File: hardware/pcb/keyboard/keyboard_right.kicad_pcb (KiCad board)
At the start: 2 copper layers, 133.8 x 110.4 mm, 118 parts, among them J1 SM04B-SRSS-TB, J2 PJ320D, J3 HRO_TYPE-C-31-M-12, J4 HRS_FH34SRJ-06S-0.5SH(50), SW29 PTS845, U1 74HC4051, U2 OPA350UA, U3 PRTR5V0U2X, U4 XC6220B331MR-G, U5 STM32G431KBTx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

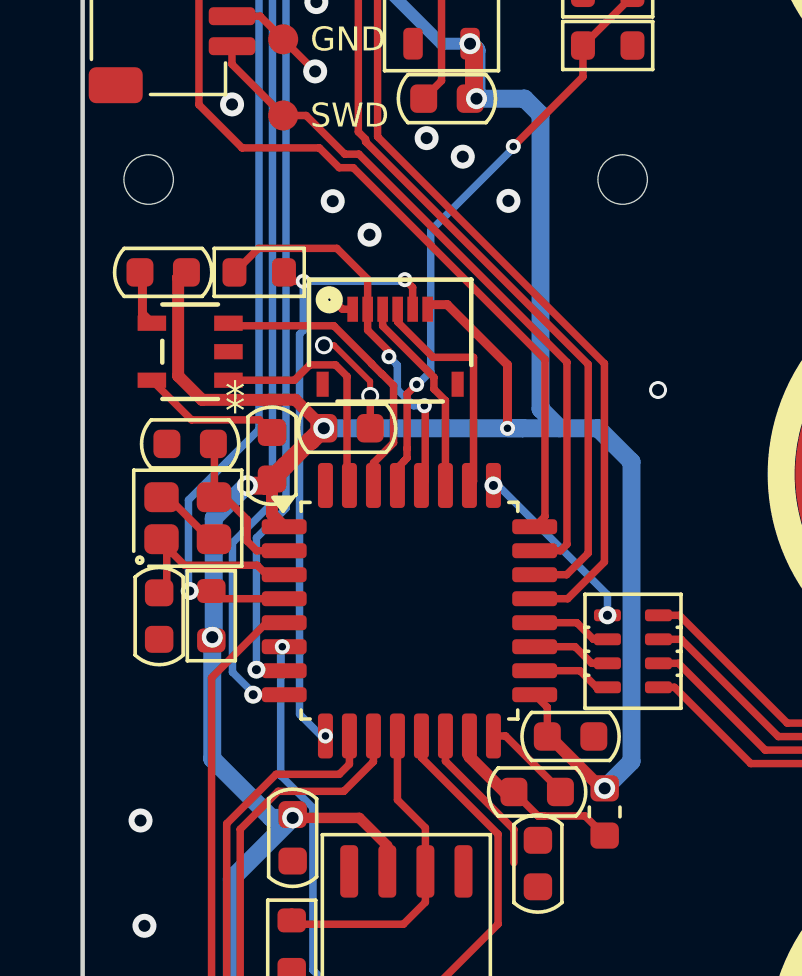
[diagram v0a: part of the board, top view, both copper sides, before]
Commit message: add pull up register for I2C.
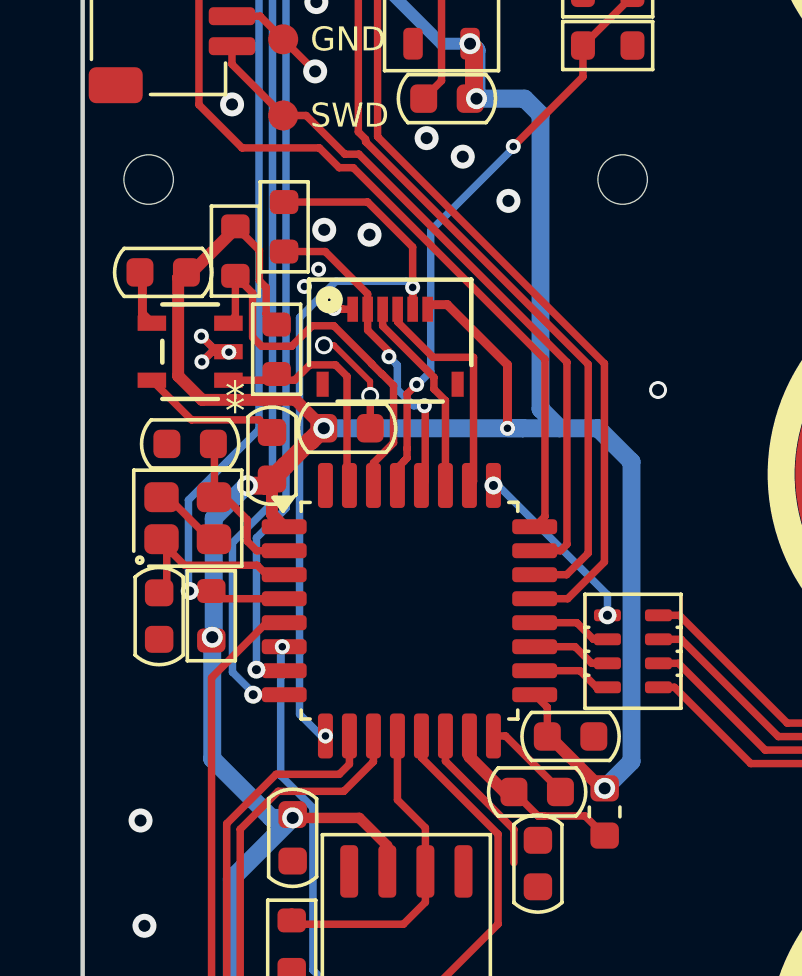
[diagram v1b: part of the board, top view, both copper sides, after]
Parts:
- added R10: 10k, PCM_Resistor_SMD_AKL:R_0603_1608Metric, F.Cu at (76.7, 76.8)
- added R9: 10k, PCM_Resistor_SMD_AKL:R_0603_1608Metric, F.Cu at (75.3, 73.6)
- moved R8 1.73 mm to (77.0, 72.8), turned to 90 degrees
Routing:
- net +3V3: track 110.8 -> 116.9 mm
- net ACCS_1: track 20.9 -> 26.4 mm, vias 3 -> 2
- net GND: track 42.7 -> 46.4 mm, vias 30 -> 35
- net I2C1_SDA: track 9.78 -> 13.5 mm
- net ACCS_4: track 13.0 -> 10.6 mm

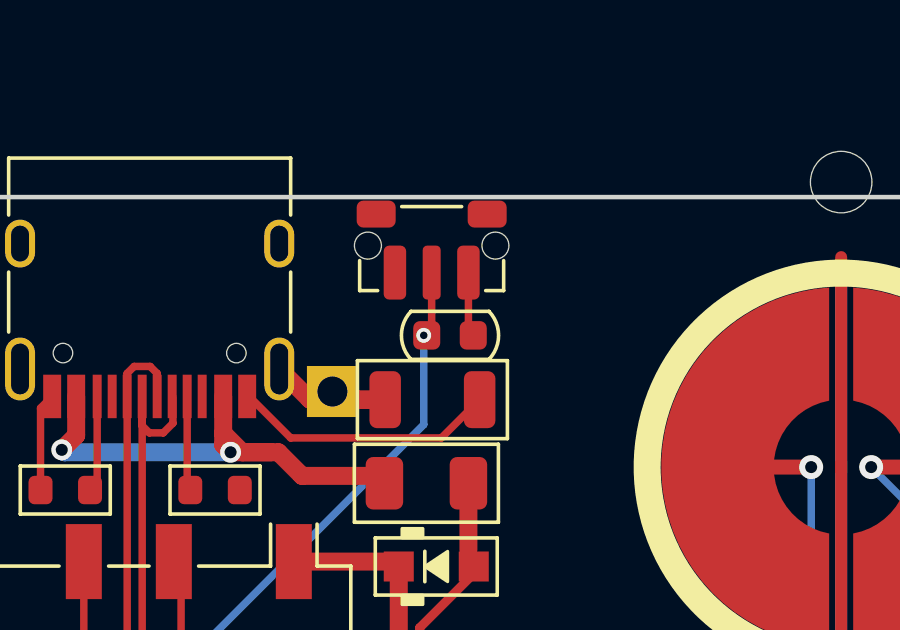
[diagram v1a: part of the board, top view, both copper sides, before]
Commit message: fix acc connection.
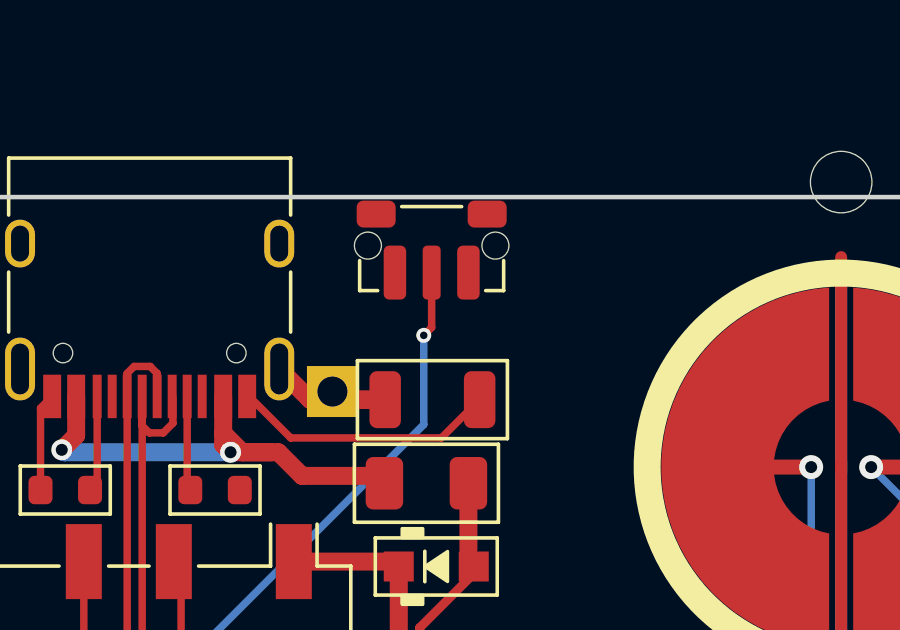
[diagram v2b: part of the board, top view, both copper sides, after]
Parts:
- removed C1: 0.1uF, PCM_Capacitor_SMD_AKL:C_0603_1608Metric
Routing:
- net GND: track 46.4 -> 44.6 mm
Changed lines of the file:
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@@
 		)
 	)
-	(footprint "PCM_Capacitor_SMD_AKL:C_0603_1608Metric"
-		(layer "F.Cu")
-		(at 86.961 38.609 180)
-		(descr "Capacitor SMD 0603 (1608 Metric), square (rectangular) end terminal, IPC_7351 nominal, (Body size source: IPC-SM-782 page 76, https://www.pcb-3d.com/wordpress/wp-content/uploads/ipc-sm-782a_amendment_1_and_2.pdf), Alternate KiCad Library")
-		(tags "capacitor")
-		(property "Reference" "C1"
-			(at 0 -1.43 180)
-			(layer "F.SilkS")
-			(hide yes)
-			(effects
-				(font
-					(size 1 1)
-					(thickness 0.15)
-				)
-			)
-		)
-		(property "Value" "0.1uF"
-			(at 0 1.43 180)
-			(layer "F.Fab")
-			(hide yes)
-			(effects
-				(font
-					(size 1 1)
-					(thickness 0.15)
-				)
-			)
-		)
-		(property "Datasheet" "~"
-			(at 0 0 180)
-			(unlocked yes)
-			(layer "F.Fab")
-			(hide yes)
-			(effects
-				(font
-					(size 1.27 1.27)
-					(thickness 0.15)
-				)
-			)
-		)
-		(property "Description" ""
-			(at 0 0 180)
-			(unlocked yes)
-			(layer "F.Fab")
-			(hide yes)
-			(effects
-				(font
-					(size 1.27 1.27)
-					(thickness 0.15)
-				)
-			)
-		)
-		(property "LCSC" "C307331"
-			(at 0 0 0)
-			(layer "F.Fab")
-			(hide yes)
-			(effects
-				(font
-					(size 1 1)
-					(thickness 0.15)
-				)
-			)
-		)
-		(property ki_fp_filters "C_*")
-		(sheetname "/")
-		(sheetfile "keyboard_right.kicad_sch")
-		(attr smd)
-		(fp_line
-			(start 1.3 -0.800002)
-			(end -1.3 -0.8)
-			(stroke
-				(width 0.12)
-				(type solid)
-			)
-			(layer "F.SilkS")
-		)
-		(fp_line
-			(start -1.3 0.800002)
-			(end 1.3 0.8)
-			(stroke
-				(width 0.12)
-				(type solid)
-			)
-			(layer "F.SilkS")
-		)
-		(fp_arc
-			(start 1.3 -0.800002)
-			(mid 1.619939 -0.000001)
-			(end 1.3 0.8)
-			(stroke
-				(width 0.12)
-				(type solid)
-			)
-			(layer "F.SilkS")
-		)
-		(fp_arc
-			(start -1.3 0.800002)
-			(mid -1.619939 0.000001)
-			(end -1.3 -0.8)
-			(stroke
-				(width 0.12)
-				(type solid)
-			)
-			(layer "F.SilkS")
-		)
-		(fp_line
-			(start 1.48 0.73)
-			(end -1.48 0.73)
-			(stroke
-				(width 0.05)
-				(type solid)
-			)
-			(layer "F.CrtYd")
-		)
-		(fp_line
-			(start 1.48 -0.73)
-			(end 1.48 0.73)
-			(stroke
-				(width 0.05)
-				(type solid)
-			)
-			(layer "F.CrtYd")
-		)
-		(fp_line
-			(start -1.48 0.73)
-			(end -1.48 -0.73)
-			(stroke
-				(width 0.05)
-				(type solid)
-			)
-			(layer "F.CrtYd")
-		)
-		(fp_line
-			(start -1.48 -0.73)
-			(end 1.48 -0.73)
-			(stroke
-				(width 0.05)
-				(type solid)
-			)
-			(layer "F.CrtYd")
-		)
-		(fp_line
-			(start 0.8 0.4)
-			(end -0.8 0.4)
-			(stroke
-				(width 0.1)
-				(type solid)
-			)
-			(layer "F.Fab")
-		)
-		(fp_line
-			(start 0.8 -0.4)
-			(end 0.8 0.4)
-			(stroke
-				(width 0.1)
-				(type solid)
-			)
-			(layer "F.Fab")
-		)
-		(fp_line
-			(start -0.8 0.4)
-			(end -0.8 -0.4)
-			(stroke
-				(width 0.1)
-				(type solid)
-			)
-			(layer "F.Fab")
-		)
-		(fp_line
-			(start -0.8 -0.4)
-			(end 0.8 -0.4)
-			(stroke
-				(width 0.1)
-				(type solid)
-			)
-			(layer "F.Fab")
-		)
-		(fp_text user "${REFERENCE}"
-			(at 0 0 180)
-			(layer "F.Fab")
-			(effects
-				(font
-					(size 0.4 0.4)
-					(thickness 0.06)
-				)
-			)
-		)
-		(pad "1" smd roundrect
-			(at -0.775 0 180)
-			(size 0.9 0.95)
-			(layers "F.Cu" "F.Mask" "F.Paste")
-			(roundrect_rratio 0.25)
-			(net 19 "GND")
-			(pintype "passive")
-		)
-		(pad "2" smd roundrect
-			(at 0.775 0 180)
-			(size 0.9 0.95)
-			(layers "F.Cu" "F.Mask" "F.Paste")
-			(roundrect_rratio 0.25)
-			(net 43 "/NRST")
-			(pintype "passive")
-		)
-		(embedded_fonts no)
-		(model "${KICAD6_3DMODEL_DIR}/Capacitor_SMD.3dshapes/C_0603_1608Metric.wrl"
-			(offset
-				(xyz 0 0 0)
-			)
-			(scale
-				(xyz 1 1 1)
-			)
-			(rotate
-				(xyz 0 0 0)
-			)
-		)
-	)
 	(footprint "ec_parts:ecs_pad_no_ring"
 		(layer "F.Cu")
@@
 	)
 	(segment
-		(start 87.575 36.517)
-		(end 87.575 38.348)
-		(width 0.25)
-		(layer "F.Cu")
-		(net 19)
-	)
-	(segment
 		(start 76.561 79.606)
 		(end 76.141 79.186)
@@
 		(width 0.25)
 		(layer "F.Cu")
+		(net 43)
+	)
+	(segment
+		(start 86.35 38.345)
+		(end 86.086 38.609)
+		(width 0.25)
+		(layer "F.Cu")

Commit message: update schema.
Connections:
- net ACCS_1 renamed PA4
- net ACCS_2 renamed PB3
- net ACCS_3 renamed PB4
- net ACCS_4 renamed PB5

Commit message: Generate production files.
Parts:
- D1: value 1N5819 -> BAT60B
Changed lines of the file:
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@@
 	(paper "A4")
 	(title_block
-		(title "Corne EEC")
-		(date "2023-07-18")
-		(rev "1.0")
-		(comment 1 "Copyright © 2023")
+		(title "Corne EEC - Keyboard Right")
+		(date "2025-09-18")
+		(rev "2.0")
 		(comment 2 "MIT License")
 	)
@@
 			)
 		)
-		(property "Value" "1N5819"
+		(property "Value" "BAT60B"
 			(at 0.1 1.9 0)
 			(layer "F.Fab")
@@
 			)
 		)
-		(property "Comment" ""
+		(property "Comment" "Alternative: 1N5819"
 			(at 0 0 0)
 			(layer "F.Fab")
@@
 			(unlocked yes)
 			(layer "F.SilkS")
+			(hide yes)
 			(effects
 				(font
@@
 			(unlocked yes)
 			(layer "F.Fab")
+			(hide yes)
 			(effects
 				(font
@@
 		(fp_text user "*"
 			(at -1.5 -1.5 180)
-			(unlocked yes)
 			(layer "F.SilkS")
 			(effects
@@
 		(fp_text user "*"
 			(at -1.5 -1.5 180)
+			(unlocked yes)
 			(layer "F.SilkS")
 			(effects
@@
 			)
 		)
-		(property "Comment" ""
+		(property "Comment" "Alternative: AP2112K"
 			(at 0 0 0)
 			(layer "F.Fab")

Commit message: Rev 2.1
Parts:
- removed H18, H19: ~, ec_parts:SMT-SO-M1.6-screwhole_only
- J4: footprint ec_parts:CONN6x1_FH34SRJ-6S-0.5SH50_HIR -> ec_parts:CONN6x1_FH12S-6S-1SH55
- moved R5 15.4 mm to (87.7, 51.3), turned to 0 degrees
- moved R4 15.4 mm to (87.7, 49.5)
- moved J4 11.1 mm to (86.5, 67.1), turned to 90 degrees
- moved C9 9.98 mm to (85.7, 59.1), turned to 90 degrees
- moved C8 6.74 mm to (83.0, 55.8)
- moved U4 6.74 mm to (82.8, 58.8)
- moved TP1 5.21 mm to (73.2, 65.1)
- moved J1 5.00 mm to (73.2, 60.7)
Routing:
- net PB6: track 19.0 -> 36.7 mm
- net VBUS: track 21.8 -> 5.80 mm
- net PB5: track 10.6 -> 26.6 mm
- net PB4: track 6.74 -> 20.6 mm, vias 0 -> 2
- net PB3: track 7.77 -> 18.9 mm, vias 0 -> 2
- net SWDIO: track 23.1 -> 33.5 mm, vias 0 -> 3
- net +3V3: track 116.9 -> 126.6 mm, vias 10 -> 9
- net GND: track 44.6 -> 36.1 mm, vias 35 -> 24
- net PA4: track 26.4 -> 33.0 mm, vias 2 -> 4
- net +5V: track 29.4 -> 24.1 mm
- net SWCLK: track 27.7 -> 30.9 mm, vias 0 -> 2
- net D-: track 53.7 -> 54.5 mm
